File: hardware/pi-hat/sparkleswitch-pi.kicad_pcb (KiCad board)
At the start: 2 copper layers, 65 x 56 mm, 26 parts, among them J1 Conn_01x02, J2 Conn_02x06_Odd_Even, P1 CONN_02X20, U1 74HCT245, U2 74HCT245, U3 74HCT245, U4 PC817, U5 PC817, U6 PC817, U7 PC817

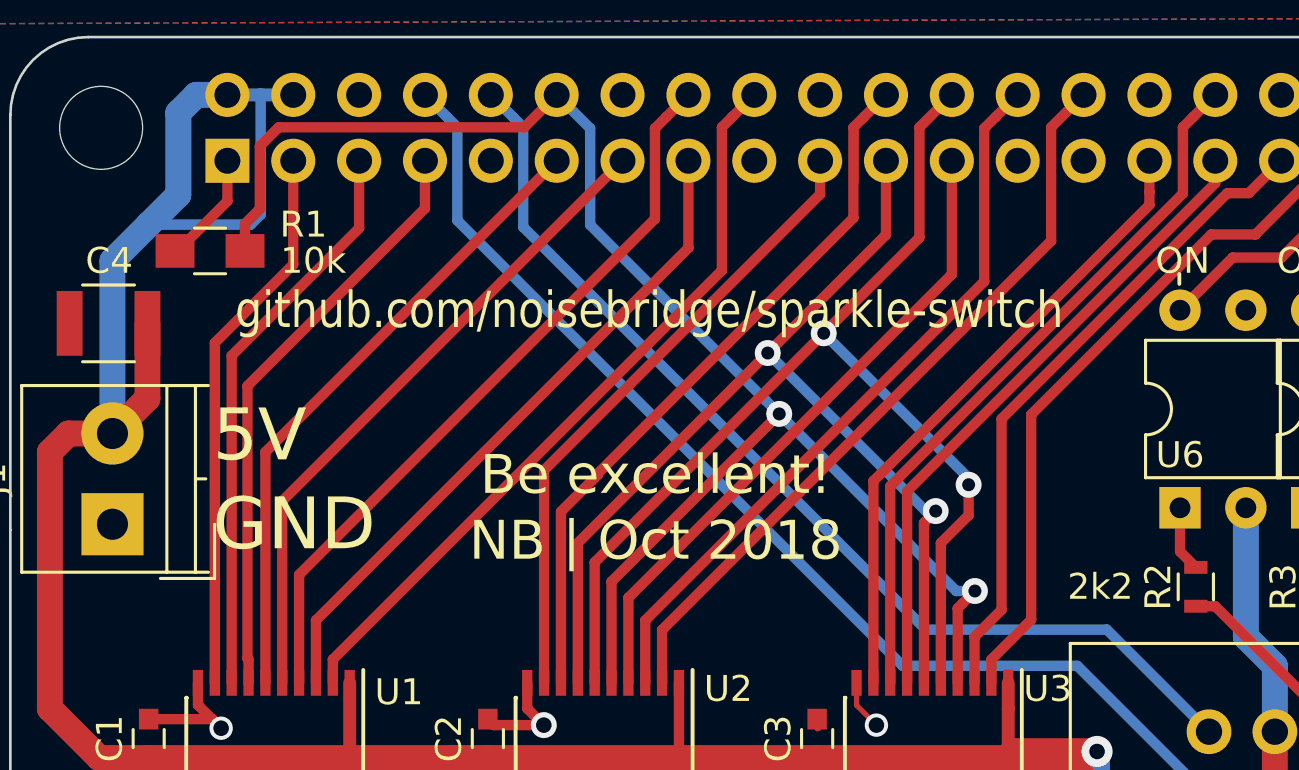
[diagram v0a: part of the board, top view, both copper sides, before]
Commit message: Use 4.7k for OptoCoupler LEDs; OE-Pullup 0805 -> 0603
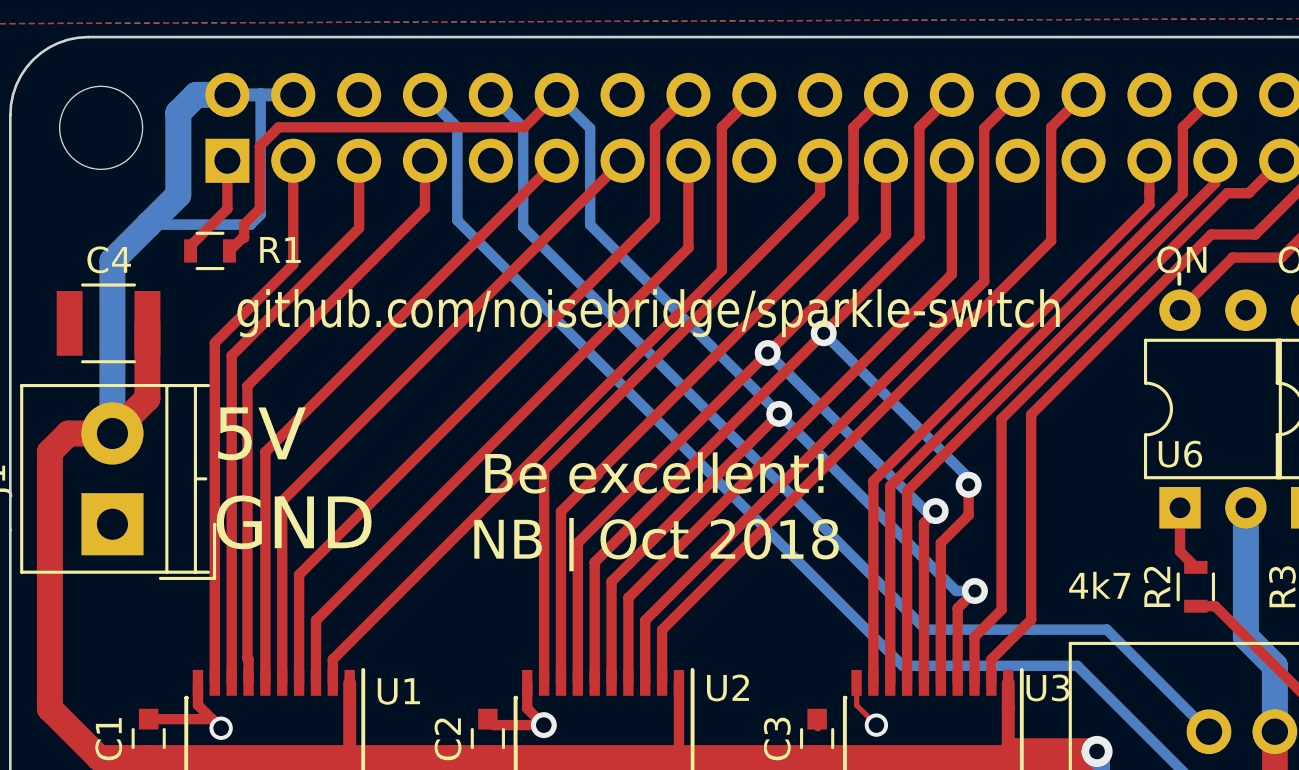
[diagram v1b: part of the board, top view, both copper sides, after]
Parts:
- R1: footprint Resistors_SMD:R_0805_HandSoldering -> Resistors_SMD:R_0603
- R2, R3, R4, R5: value 2k2 -> 4k7
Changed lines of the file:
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@@
-(kicad_pcb (version 20171130) (host pcbnew "(6.0.0-rc1-dev-995-gf1b2855e8)")
+(kicad_pcb (version 20171130) (host pcbnew "(6.0.0-rc1-dev-1037-gd95372436)")
   (general
     (thickness 1.6)
     (drawings 60)
-    (tracks 417)
+    (tracks 419)
     (zones 0)
     (modules 26)
@@
   )
   (setup
-    (last_trace_width 1)
+    (last_trace_width 0.4)
     (user_trace_width 0.4)
     (user_trace_width 0.5)
@@
     (uvia_drill 0.1)
   )
+  (module Resistors_SMD:R_0603 (layer F.Cu)
+    (at 207.7 102.248 180)
+    (descr "Resistor SMD 0603, reflow soldering, Vishay (see dcrcw.pdf)")
+    (tags "resistor 0603")
+    (attr smd)
+    (fp_text reference R1 (at -2.714 0 180) (layer F.SilkS)
+      (effects (font (size 1 1) (thickness 0.15)))
+    )
+    (fp_text value 10k (at 0 1.5 180) (layer F.Fab)
+      (effects (font (size 1 1) (thickness 0.15)))
+    )
+    (fp_line (start 1.25 0.7) (end -1.25 0.7) (layer F.CrtYd) (width 0.05))
+    (fp_line (start 1.25 0.7) (end 1.25 -0.7) (layer F.CrtYd) (width 0.05))
+    (fp_line (start -1.25 -0.7) (end -1.25 0.7) (layer F.CrtYd) (width 0.05))
+    (fp_line (start -1.25 -0.7) (end 1.25 -0.7) (layer F.CrtYd) (width 0.05))
+    (fp_line (start -0.5 -0.68) (end 0.5 -0.68) (layer F.SilkS) (width 0.12))
+    (fp_line (start 0.5 0.68) (end -0.5 0.68) (layer F.SilkS) (width 0.12))
+    (fp_line (start -0.8 -0.4) (end 0.8 -0.4) (layer F.Fab) (width 0.1))
+    (fp_line (start 0.8 -0.4) (end 0.8 0.4) (layer F.Fab) (width 0.1))
+    (fp_line (start 0.8 0.4) (end -0.8 0.4) (layer F.Fab) (width 0.1))
+    (fp_line (start -0.8 0.4) (end -0.8 -0.4) (layer F.Fab) (width 0.1))
+    (fp_text user %R (at 0 0 180) (layer F.Fab)
+      (effects (font (size 0.4 0.4) (thickness 0.075)))
+    )
+    (pad 2 smd rect (at 0.75 0 180) (size 0.5 0.9) (layers F.Cu F.Paste F.Mask)
+      (net 3 "Net-(P1-Pad1)"))
+    (pad 1 smd rect (at -0.75 0 180) (size 0.5 0.9) (layers F.Cu F.Paste F.Mask)
+      (net 6 OE))
+    (model ${KISYS3DMOD}/Resistors_SMD.3dshapes/R_0603.wrl
+      (at (xyz 0 0 0))
+      (scale (xyz 1 1 1))
+      (rotate (xyz 0 0 0))
+    )
+  )
   (module Capacitors_SMD:C_0603 (layer F.Cu)
     (at 231.115 121.056 90)
@@
       (effects (font (size 1 1) (thickness 0.15)))
     )
-    (fp_text value 2k2 (at 0 1.5 270) (layer F.Fab)
+    (fp_text value 4k7 (at 0 1.5 270) (layer F.Fab)
       (effects (font (size 1 1) (thickness 0.15)))
     )
@@
       (effects (font (size 1 1) (thickness 0.15)))
     )
-    (fp_text value 2k2 (at 0 -3.683 180) (layer F.SilkS)
+    (fp_text value 4k7 (at 0 -3.683 180) (layer F.SilkS)
       (effects (font (size 1 1) (thickness 0.15)))
     )
@@
       (effects (font (size 1 1) (thickness 0.15)))
     )
-    (fp_text value 2k2 (at 0 1.5 90) (layer F.Fab)
+    (fp_text value 4k7 (at 0 1.5 90) (layer F.Fab)
       (effects (font (size 1 1) (thickness 0.15)))
     )
@@
       (effects (font (size 1 1) (thickness 0.15)))
     )
-    (fp_text value 2k2 (at 0 1.5 90) (layer F.Fab)
+    (fp_text value 4k7 (at 0 1.5 90) (layer F.Fab)
       (effects (font (size 1 1) (thickness 0.15)))
     )
@@
       (net 2 VCC))
     (model ${KISYS3DMOD}/Housings_SSOP.3dshapes/SSOP-20_4.4x6.5mm_Pitch0.65mm.wrl
-      (at (xyz 0 0 0))
-      (scale (xyz 1 1 1))
-      (rotate (xyz 0 0 0))
-    )
-  )
-  (module Resistors_SMD:R_0805_HandSoldering (layer F.Cu)
-    (at 207.7 102.248 180)
-    (descr "Resistor SMD 0805, hand soldering")
-    (tags "resistor 0805")
-    (attr smd)
-    (fp_text reference R1 (at -3.603 1.016 180) (layer F.SilkS)
-      (effects (font (size 1 1) (thickness 0.15)))
-    )
-    (fp_text value 10k (at -3.984 -0.381 180) (layer F.SilkS)
-      (effects (font (size 1 1) (thickness 0.15)))
-    )
-    (fp_line (start 2.35 0.9) (end -2.35 0.9) (layer F.CrtYd) (width 0.05))
-    (fp_line (start 2.35 0.9) (end 2.35 -0.9) (layer F.CrtYd) (width 0.05))
-    (fp_line (start -2.35 -0.9) (end -2.35 0.9) (layer F.CrtYd) (width 0.05))
-    (fp_line (start -2.35 -0.9) (end 2.35 -0.9) (layer F.CrtYd) (width 0.05))
-    (fp_line (start -0.6 -0.88) (end 0.6 -0.88) (layer F.SilkS) (width 0.12))
-    (fp_line (start 0.6 0.88) (end -0.6 0.88) (layer F.SilkS) (width 0.12))
-    (fp_line (start -1 -0.62) (end 1 -0.62) (layer F.Fab) (width 0.1))
-    (fp_line (start 1 -0.62) (end 1 0.62) (layer F.Fab) (width 0.1))
-    (fp_line (start 1 0.62) (end -1 0.62) (layer F.Fab) (width 0.1))
-    (fp_line (start -1 0.62) (end -1 -0.62) (layer F.Fab) (width 0.1))
-    (fp_text user %R (at 0 0 180) (layer F.Fab)
-      (effects (font (size 0.5 0.5) (thickness 0.075)))
-    )
-    (pad 2 smd rect (at 1.35 0 180) (size 1.5 1.3) (layers F.Cu F.Paste F.Mask)
-      (net 3 "Net-(P1-Pad1)"))
-    (pad 1 smd rect (at -1.35 0 180) (size 1.5 1.3) (layers F.Cu F.Paste F.Mask)
-      (net 6 OE))
-    (model ${KISYS3DMOD}/Resistors_SMD.3dshapes/R_0805.wrl
       (at (xyz 0 0 0))
       (scale (xyz 1 1 1))
@@
   (gr_line (start 203 150) (end 262 150) (layer Edge.Cuts) (width 0.1))
   (gr_line (start 200 131) (end 200 147) (layer Edge.Cuts) (width 0.1))
-  (segment (start 221.205 118.906) (end 221.205 119.206) (width 0.2) (layer F.Cu) (net 14))
   (segment (start 231.166 120.675) (end 231.115 120.675) (width 0.2) (layer F.Cu) (net 1))
   (segment (start 232.635 118.906) (end 232.635 119.206) (width 0.2) (layer F.Cu) (net 1))
@@
   (segment (start 218.415 121.806) (end 217.04 121.806) (width 1) (layer F.Cu) (net 2))
   (segment (start 258.928 120.79) (end 258.928 123.33) (width 1) (layer F.Cu) (net 2))
-  (segment (start 206.45 102.248) (end 206.35 102.248) (width 0.4) (layer F.Cu) (net 3))
-  (segment (start 208.37 100.328) (end 206.45 102.248) (width 0.4) (layer F.Cu) (net 3))
-  (segment (start 208.37 98.77) (end 208.37 100.328) (width 0.4) (layer F.Cu) (net 3))
+  (segment (start 206.95 102.048) (end 206.95 102.248) (width 0.4) (layer F.Cu) (net 3))
+  (segment (start 208.37 100.628) (end 206.95 102.048) (width 0.4) (layer F.Cu) (net 3))
+  (segment (start 208.37 98.77) (end 208.37 100.628) (width 0.4) (layer F.Cu) (net 3))
   (via (at 231.369 105.423) (size 1) (drill 0.5) (layers F.Cu B.Cu) (net 4))
   (segment (start 236.31 96.23) (end 235.059999 97.480001) (width 0.4) (layer F.Cu) (net 4))
@@
   (segment (start 236.483399 115.363399) (end 237.200409 115.363399) (width 0.4) (layer B.Cu) (net 6))
   (segment (start 229.653096 108.533096) (end 236.483399 115.363399) (width 0.4) (layer B.Cu) (net 6))
-  (segment (start 209.05 101.198) (end 209.05 102.248) (width 0.4) (layer F.Cu) (net 6))
-  (segment (start 209.620001 100.627999) (end 209.05 101.198) (width 0.4) (layer F.Cu) (net 6))
-  (segment (start 209.620001 98.209997) (end 209.620001 100.627999) (width 0.4) (layer F.Cu) (net 6))
-  (segment (start 219.819999 97.480001) (end 210.349997 97.480001) (width 0.4) (layer F.Cu) (net 6))
-  (segment (start 210.349997 97.480001) (end 209.620001 98.209997) (width 0.4) (layer F.Cu) (net 6))
-  (segment (start 221.07 96.23) (end 219.819999 97.480001) (width 0.4) (layer F.Cu) (net 6))
   (segment (start 223.185 115.001192) (end 223.185 118.906) (width 0.4) (layer F.Cu) (net 6))
   (segment (start 229.653096 108.533096) (end 223.185 115.001192) (width 0.4) (layer F.Cu) (net 6))
+  (segment (start 209.017 101.74) (end 208.958 101.74) (width 0.4) (layer F.Cu) (net 6))
+  (segment (start 219.819999 97.480001) (end 210.349997 97.480001) (width 0.4) (layer F.Cu) (net 6))
+  (segment (start 221.07 96.23) (end 219.819999 97.480001) (width 0.4) (layer F.Cu) (net 6))
+  (segment (start 210.349997 97.480001) (end 209.620001 98.209997) (width 0.4) (layer F.Cu) (net 6))
+  (segment (start 209.620001 98.209997) (end 209.620001 100.627999) (width 0.4) (layer F.Cu) (net 6))
+  (segment (start 208.958 101.74) (end 208.45 102.248) (width 0.4) (layer F.Cu) (net 6))
+  (segment (start 209.620001 100.627999) (end 209.017 101.231) (width 0.4) (layer F.Cu) (net 6))
+  (segment (start 209.017 101.231) (end 209.017 101.74) (width 0.4) (layer F.Cu) (net 6))
   (segment (start 208.535 118.906) (end 208.535 106.286) (width 0.4) (layer F.Cu) (net 7))
   (segment (start 213.45 101.371) (end 213.45 98.77) (width 0.4) (layer F.Cu) (net 7))
@@
   (segment (start 210.485 111.895) (end 210.485 118.906) (width 0.4) (layer F.Cu) (net 13))
   (segment (start 223.61 98.77) (end 210.485 111.895) (width 0.4) (layer F.Cu) (net 13))
+  (segment (start 221.205 118.906) (end 221.205 119.206) (width 0.2) (layer F.Cu) (net 14))
   (segment (start 232.619999 97.380001) (end 232.920001 97.079999) (width 0.2) (layer F.Cu) (net 14))
   (segment (start 232.619999 99.600001) (end 232.619999 97.380001) (width 0.2) (layer F.Cu) (net 14))
